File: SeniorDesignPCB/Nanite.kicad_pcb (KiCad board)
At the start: 2 copper layers, 25 parts, among them U1 4017, U2 TLC555

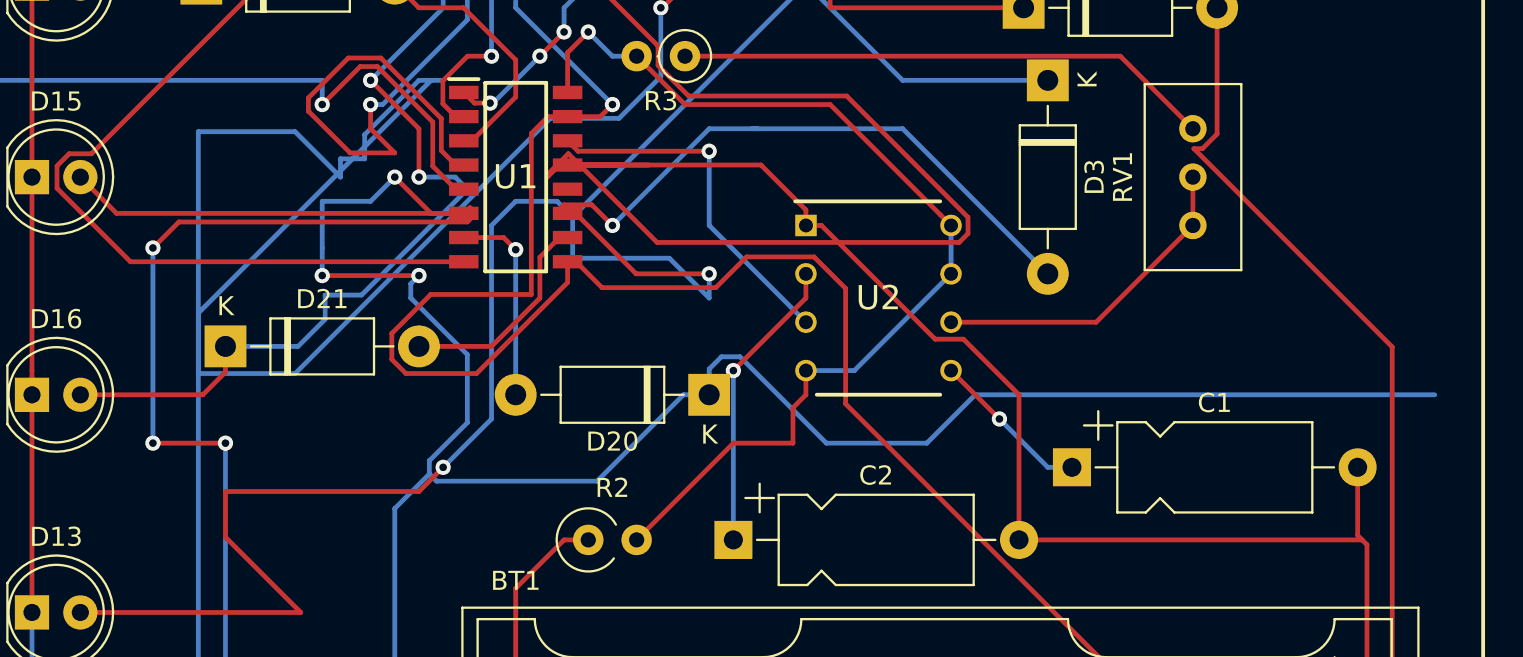
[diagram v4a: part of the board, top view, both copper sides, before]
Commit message: fixing up DRC issues
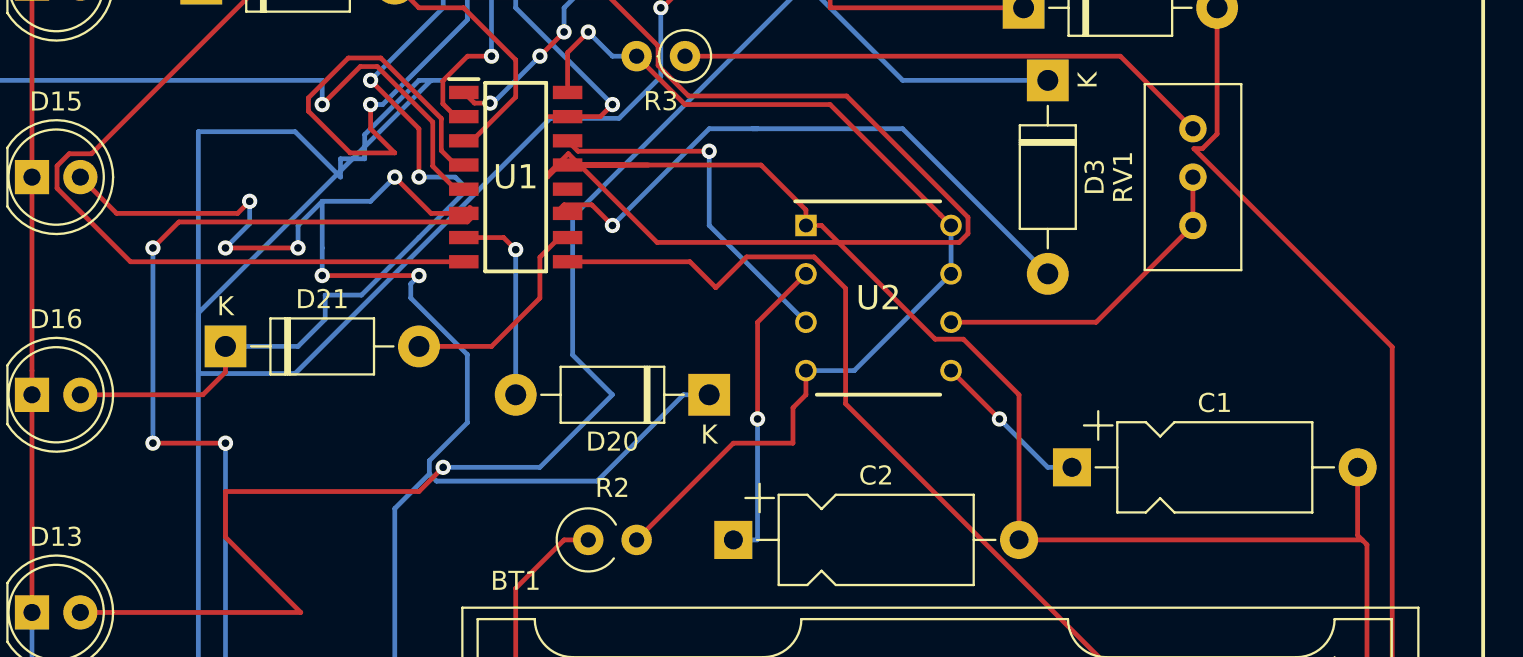
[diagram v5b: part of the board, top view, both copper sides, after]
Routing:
- net Net-(D15-Pad2): track 126.3 -> 80.7 mm, vias 3 -> 6
- net Net-(D14-Pad2): track 116.8 -> 84.9 mm
- net Net-(D13-Pad2): track 115.5 -> 97.0 mm, vias 2 -> 1
- net Net-(D5-Pad2): track 49.1 -> 50.8 mm
- net Net-(C2-Pad1): track 15.5 -> 16.3 mm
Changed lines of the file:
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@@
     (thickness 1.6)
     (drawings 4)
-    (tracks 335)
+    (tracks 323)
     (zones 0)
     (modules 25)
@@
   (segment (start 107.95 77.47) (end 116.92 77.47) (width 0.25) (layer F.Cu) (net 3))
   (segment (start 119.81 89.535) (end 120.835 89.535) (width 0.25) (layer F.Cu) (net 3))
-  (segment (start 118.92999 98.8736) (end 118.92999 90.41501) (width 0.25) (layer F.Cu) (net 3))
-  (segment (start 113.647398 98.8736) (end 118.92999 98.8736) (width 0.25) (layer F.Cu) (net 3))
-  (segment (start 118.92999 90.41501) (end 119.81 89.535) (width 0.25) (layer F.Cu) (net 3))
-  (segment (start 111.604999 100.915999) (end 113.647398 98.8736) (width 0.25) (layer F.Cu) (net 3))
-  (segment (start 111.604999 102.284001) (end 111.604999 100.915999) (width 0.25) (layer F.Cu) (net 3))
-  (segment (start 112.345999 103.025001) (end 111.604999 102.284001) (width 0.25) (layer F.Cu) (net 3))
-  (segment (start 116.051409 103.025001) (end 112.345999 103.025001) (width 0.25) (layer F.Cu) (net 3))
-  (segment (start 120.835 98.24141) (end 116.051409 103.025001) (width 0.25) (layer F.Cu) (net 3))
-  (segment (start 120.835 97.155) (end 120.835 98.24141) (width 0.25) (layer F.Cu) (net 3))
   (segment (start 118.11 80.01) (end 118.11 83.82) (width 0.25) (layer B.Cu) (net 3))
   (via (at 123.19 88.9) (size 0.8) (drill 0.4) (layers F.Cu B.Cu) (net 3))
@@
   (segment (start 113.03 95.88641) (end 115.57 93.34641) (width 0.25) (layer B.Cu) (net 7))
   (segment (start 115.57 93.34641) (end 115.7564 93.16001) (width 0.25) (layer B.Cu) (net 7))
-  (segment (start 97.155 94.615) (end 115.385 94.615) (width 0.25) (layer F.Cu) (net 8))
   (segment (start 95.25 92.71) (end 97.155 94.615) (width 0.25) (layer F.Cu) (net 8))
   (segment (start 128.27 104.14) (end 126.92 104.14) (width 0.25) (layer B.Cu) (net 8))
@@
   (segment (start 107.95 97.88) (end 107.95 96.43) (width 0.25) (layer B.Cu) (net 8))
   (segment (start 107.95 96.43) (end 107.95 93.98) (width 0.25) (layer B.Cu) (net 8))
-  (via (at 111.76 92.71) (size 0.8) (drill 0.4) (layers F.Cu B.Cu) (net 8))
+  (segment (start 111.76 110.113) (end 113.574999 108.298001) (width 0.25) (layer B.Cu) (net 8))
+  (segment (start 111.76 123.19) (end 111.76 110.113) (width 0.25) (layer B.Cu) (net 8))
+  (segment (start 97.155 94.615) (end 103.505 94.615) (width 0.25) (layer F.Cu) (net 8))
+  (via (at 104.14 93.98) (size 0.8) (drill 0.4) (layers F.Cu B.Cu) (net 8))
+  (segment (start 103.505 94.615) (end 104.14 93.98) (width 0.25) (layer F.Cu) (net 8))
+  (via (at 102.87 96.43) (size 0.8) (drill 0.4) (layers F.Cu B.Cu) (net 8))
+  (segment (start 104.14 93.98) (end 104.14 95.16) (width 0.25) (layer B.Cu) (net 8))
+  (segment (start 104.14 95.16) (end 102.87 96.43) (width 0.25) (layer B.Cu) (net 8))
+  (via (at 106.68 96.43) (size 0.8) (drill 0.4) (layers F.Cu B.Cu) (net 8))
+  (segment (start 102.87 96.43) (end 106.68 96.43) (width 0.25) (layer F.Cu) (net 8))
+  (segment (start 106.68 95.25) (end 107.95 93.98) (width 0.25) (layer B.Cu) (net 8))
+  (segment (start 106.68 96.43) (end 106.68 95.25) (width 0.25) (layer B.Cu) (net 8))
   (segment (start 107.95 93.98) (end 110.49 93.98) (width 0.25) (layer B.Cu) (net 8))
   (segment (start 110.49 93.98) (end 111.76 92.71) (width 0.25) (layer B.Cu) (net 8))
-  (segment (start 113.665 94.615) (end 115.385 94.615) (width 0.25) (layer F.Cu) (net 8))
+  (via (at 111.76 92.71) (size 0.8) (drill 0.4) (layers F.Cu B.Cu) (net 8))
   (segment (start 111.76 92.71) (end 113.665 94.615) (width 0.25) (layer F.Cu) (net 8))
-  (segment (start 128.27 102.79) (end 128.27 104.14) (width 0.25) (layer B.Cu) (net 8))
-  (segment (start 128.915001 102.144999) (end 128.27 102.79) (width 0.25) (layer B.Cu) (net 8))
-  (segment (start 129.888001 102.144999) (end 128.915001 102.144999) (width 0.25) (layer B.Cu) (net 8))
-  (segment (start 166.37 104.14) (end 142.24 104.14) (width 0.25) (layer B.Cu) (net 8))
-  (segment (start 142.24 104.14) (end 139.7 106.68) (width 0.25) (layer B.Cu) (net 8))
-  (segment (start 139.7 106.68) (end 134.423002 106.68) (width 0.25) (layer B.Cu) (net 8))
-  (segment (start 134.423002 106.68) (end 129.888001 102.144999) (width 0.25) (layer B.Cu) (net 8))
-  (segment (start 111.76 110.113) (end 113.574999 108.298001) (width 0.25) (layer B.Cu) (net 8))
-  (segment (start 111.76 123.19) (end 111.76 110.113) (width 0.25) (layer B.Cu) (net 8))
   (segment (start 95.25 115.57) (end 106.824999 115.57) (width 0.25) (layer F.Cu) (net 9))
   (segment (start 102.87 111.615001) (end 102.87 109.22) (width 0.25) (layer F.Cu) (net 9))
@@
   (via (at 114.3 107.95) (size 0.8) (drill 0.4) (layers F.Cu B.Cu) (net 9))
   (segment (start 113.03 109.22) (end 114.3 107.95) (width 0.25) (layer F.Cu) (net 9))
-  (segment (start 114.3 107.95) (end 116.84 105.41) (width 0.25) (layer B.Cu) (net 9))
-  (segment (start 116.84 105.41) (end 116.84 95.25) (width 0.25) (layer B.Cu) (net 9))
-  (segment (start 116.84 95.25) (end 118.11 93.98) (width 0.25) (layer B.Cu) (net 9))
-  (segment (start 120.28002 93.98) (end 121.10001 94.79999) (width 0.25) (layer B.Cu) (net 9))
-  (segment (start 118.11 93.98) (end 120.28002 93.98) (width 0.25) (layer B.Cu) (net 9))
   (segment (start 121.10001 94.79999) (end 121.10001 96.97001) (width 0.25) (layer B.Cu) (net 9))
-  (segment (start 121.26 94.615) (end 124.435 97.79) (width 0.25) (layer F.Cu) (net 9))
-  (segment (start 120.835 94.615) (end 121.26 94.615) (width 0.25) (layer F.Cu) (net 9))
-  (via (at 128.27 97.79) (size 0.8) (drill 0.4) (layers F.Cu B.Cu) (net 9))
-  (segment (start 124.435 97.79) (end 128.27 97.79) (width 0.25) (layer F.Cu) (net 9))
-  (segment (start 128.27 97.79) (end 128.27 99.06) (width 0.25) (layer B.Cu) (net 9))
-  (segment (start 126.18001 96.97001) (end 121.10001 96.97001) (width 0.25) (layer B.Cu) (net 9))
-  (segment (start 128.27 99.06) (end 126.18001 96.97001) (width 0.25) (layer B.Cu) (net 9))
+  (segment (start 120.835 94.615) (end 121.26 94.615) (width 0.25) (layer F.Cu) (net 25))
   (segment (start 138.43 87.63) (end 146.05 87.63) (width 0.25) (layer B.Cu) (net 9))
   (segment (start 133.35 82.55) (end 138.43 87.63) (width 0.25) (layer B.Cu) (net 9))
+  (segment (start 114.3 107.95) (end 119.38 107.95) (width 0.25) (layer B.Cu) (net 9))
+  (segment (start 119.38 107.95) (end 123.19 104.14) (width 0.25) (layer B.Cu) (net 9))
+  (segment (start 121.10001 102.05001) (end 121.10001 96.97001) (width 0.25) (layer B.Cu) (net 9))
+  (segment (start 123.19 104.14) (end 121.10001 102.05001) (width 0.25) (layer B.Cu) (net 9))
   (segment (start 95.25 82.55) (end 101.6 82.55) (width 0.25) (layer F.Cu) (net 10))
   (via (at 116.84 86.36) (size 0.8) (drill 0.4) (layers F.Cu B.Cu) (net 11))
@@
   (segment (start 146.05 107.95) (end 147.32 107.95) (width 0.25) (layer B.Cu) (net 19))
   (segment (start 143.51 105.41) (end 146.05 107.95) (width 0.25) (layer B.Cu) (net 19))
-  (via (at 129.54 102.87) (size 0.8) (drill 0.4) (layers F.Cu B.Cu) (net 20))
-  (segment (start 133.35 97.79) (end 133.35 99.06) (width 0.25) (layer F.Cu) (net 20))
-  (segment (start 133.35 99.06) (end 129.54 102.87) (width 0.25) (layer F.Cu) (net 20))
-  (segment (start 129.54 102.87) (end 129.54 111.76) (width 0.25) (layer B.Cu) (net 20))
+  (via (at 130.81 105.41) (size 0.8) (drill 0.4) (layers F.Cu B.Cu) (net 20))
+  (segment (start 133.35 97.79) (end 130.81 100.33) (width 0.25) (layer F.Cu) (net 20))
+  (segment (start 130.81 100.33) (end 130.81 105.41) (width 0.25) (layer F.Cu) (net 20))
+  (segment (start 130.79 111.76) (end 129.54 111.76) (width 0.25) (layer B.Cu) (net 20))
+  (segment (start 130.81 111.74) (end 130.79 111.76) (width 0.25) (layer B.Cu) (net 20))
+  (segment (start 130.81 105.41) (end 130.81 111.74) (width 0.25) (layer B.Cu) (net 20))
   (segment (start 95.25 125.73) (end 101.6 119.38) (width 0.25) (layer B.Cu) (net 21))
   (segment (start 101.444999 119.224999) (end 101.444999 90.325001) (width 0.25) (layer B.Cu) (net 21))
@@
   (segment (start 100.42499 95.06501) (end 115.5714 95.06501) (width 0.25) (layer F.Cu) (net 24))
   (segment (start 99.06 96.43) (end 100.42499 95.06501) (width 0.25) (layer F.Cu) (net 24))
+  (segment (start 113.665 94.615) (end 115.385 94.615) (width 0.25) (layer F.Cu) (net 24))
   (segment (start 146.05 97.79) (end 138.43 90.17) (width 0.25) (layer B.Cu) (net 25))
   (via (at 123.19 95.25) (size 0.8) (drill 0.4) (layers F.Cu B.Cu) (net 25))
@@
   (segment (start 133.777201 96.899999) (end 130.233003 96.899999) (width 0.25) (layer F.Cu) (net 26))
   (segment (start 135.43359 104.614592) (end 135.43359 98.556388) (width 0.25) (layer F.Cu) (net 26))
-  (segment (start 128.618001 98.515001) (end 122.645011 98.515001) (width 0.25) (layer F.Cu) (net 26))
   (segment (start 154.063999 123.245001) (end 135.43359 104.614592) (width 0.25) (layer F.Cu) (net 26))
   (segment (start 163.446001 123.245001) (end 154.063999 123.245001) (width 0.25) (layer F.Cu) (net 26))
@@
   (segment (start 164.135001 101.628399) (end 164.135001 122.556001) (width 0.25) (layer F.Cu) (net 26))
   (segment (start 154.171601 91.215001) (end 153.721603 91.215001) (width 0.25) (layer F.Cu) (net 26))
-  (segment (start 122.645011 98.515001) (end 121.28501 97.155) (width 0.25) (layer F.Cu) (net 26))
   (segment (start 154.94 90.446602) (end 154.171601 91.215001) (width 0.25) (layer F.Cu) (net 26))
   (segment (start 153.721603 91.215001) (end 164.135001 101.628399) (width 0.25) (layer F.Cu) (net 26))
   (segment (start 154.94 83.82) (end 154.94 90.446602) (width 0.25) (layer F.Cu) (net 26))
+  (segment (start 127.258 97.155) (end 128.618001 98.515001) (width 0.25) (layer F.Cu) (net 26))
+  (segment (start 120.835 97.155) (end 127.258 97.155) (width 0.25) (layer F.Cu) (net 26))
 )

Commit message: Done with pcb
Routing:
- net Net-(R3-Pad1): track 28.2 -> 36.9 mm
- net Net-(D15-Pad2): track 80.7 -> 73.7 mm, vias 6 -> 5
- net Net-(D5-Pad2): track 50.8 -> 49.1 mm
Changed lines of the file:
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@@
     (thickness 1.6)
     (drawings 4)
-    (tracks 323)
+    (tracks 322)
     (zones 0)
     (modules 25)
@@
   (segment (start 92.71 125.73) (end 92.71 115.57) (width 0.25) (layer B.Cu) (net 4))
   (segment (start 149.86 86.36) (end 153.67 90.17) (width 0.25) (layer F.Cu) (net 5))
-  (segment (start 127 86.36) (end 149.86 86.36) (width 0.25) (layer F.Cu) (net 5))
+  (segment (start 127 86.36) (end 139.7 86.36) (width 0.25) (layer F.Cu) (net 5))
+  (segment (start 139.7 86.36) (end 139.7 88.9) (width 0.25) (layer F.Cu) (net 5))
+  (segment (start 139.7 88.9) (end 142.24 91.44) (width 0.25) (layer F.Cu) (net 5))
+  (segment (start 142.24 91.44) (end 149.86 91.44) (width 0.25) (layer F.Cu) (net 5))
+  (segment (start 149.86 91.44) (end 149.86 86.36) (width 0.25) (layer F.Cu) (net 5))
   (segment (start 148.59 100.33) (end 153.67 95.25) (width 0.25) (layer F.Cu) (net 6))
   (segment (start 140.97 100.33) (end 148.59 100.33) (width 0.25) (layer F.Cu) (net 6))
@@
   (segment (start 115.57 102.030998) (end 112.599002 99.06) (width 0.25) (layer B.Cu) (net 8))
   (segment (start 115.57 105.606998) (end 115.57 102.030998) (width 0.25) (layer B.Cu) (net 8))
-  (via (at 113.03 97.88) (size 0.8) (drill 0.4) (layers F.Cu B.Cu) (net 8))
-  (segment (start 112.599002 99.06) (end 112.599002 98.310998) (width 0.25) (layer B.Cu) (net 8))
-  (segment (start 112.599002 98.310998) (end 113.03 97.88) (width 0.25) (layer B.Cu) (net 8))
-  (segment (start 113.03 97.88) (end 108.04 97.88) (width 0.25) (layer F.Cu) (net 8))
-  (via (at 107.95 97.88) (size 0.8) (drill 0.4) (layers F.Cu B.Cu) (net 8))
   (segment (start 108.04 97.88) (end 107.95 97.88) (width 0.25) (layer F.Cu) (net 8))
-  (segment (start 107.95 97.88) (end 107.95 96.43) (width 0.25) (layer B.Cu) (net 8))
-  (segment (start 107.95 96.43) (end 107.95 93.98) (width 0.25) (layer B.Cu) (net 8))
   (segment (start 111.76 110.113) (end 113.574999 108.298001) (width 0.25) (layer B.Cu) (net 8))
   (segment (start 111.76 123.19) (end 111.76 110.113) (width 0.25) (layer B.Cu) (net 8))
@@
   (segment (start 106.68 95.25) (end 107.95 93.98) (width 0.25) (layer B.Cu) (net 8))
   (segment (start 106.68 96.43) (end 106.68 95.25) (width 0.25) (layer B.Cu) (net 8))
-  (segment (start 107.95 93.98) (end 110.49 93.98) (width 0.25) (layer B.Cu) (net 8))
-  (segment (start 110.49 93.98) (end 111.76 92.71) (width 0.25) (layer B.Cu) (net 8))
-  (via (at 111.76 92.71) (size 0.8) (drill 0.4) (layers F.Cu B.Cu) (net 8))
-  (segment (start 111.76 92.71) (end 113.665 94.615) (width 0.25) (layer F.Cu) (net 8))
+  (via (at 113.03 97.88) (size 0.8) (drill 0.4) (layers F.Cu B.Cu) (net 8))
+  (segment (start 112.599002 98.310998) (end 113.03 97.88) (width 0.25) (layer B.Cu) (net 8))
+  (segment (start 112.599002 99.06) (end 112.599002 98.310998) (width 0.25) (layer B.Cu) (net 8))
+  (segment (start 113.03 97.88) (end 108.04 97.88) (width 0.25) (layer F.Cu) (net 8))
+  (via (at 107.95 97.88) (size 0.8) (drill 0.4) (layers F.Cu B.Cu) (net 8))
+  (segment (start 107.95 97.88) (end 107.95 96.43) (width 0.25) (layer B.Cu) (net 8))
+  (segment (start 107.95 96.43) (end 107.95 93.98) (width 0.25) (layer B.Cu) (net 8))
   (segment (start 95.25 115.57) (end 106.824999 115.57) (width 0.25) (layer F.Cu) (net 9))
   (segment (start 102.87 111.615001) (end 102.87 109.22) (width 0.25) (layer F.Cu) (net 9))
@@
   (segment (start 100.42499 95.06501) (end 115.5714 95.06501) (width 0.25) (layer F.Cu) (net 24))
   (segment (start 99.06 96.43) (end 100.42499 95.06501) (width 0.25) (layer F.Cu) (net 24))
-  (segment (start 113.665 94.615) (end 115.385 94.615) (width 0.25) (layer F.Cu) (net 24))
   (segment (start 146.05 97.79) (end 138.43 90.17) (width 0.25) (layer B.Cu) (net 25))
   (via (at 123.19 95.25) (size 0.8) (drill 0.4) (layers F.Cu B.Cu) (net 25))
